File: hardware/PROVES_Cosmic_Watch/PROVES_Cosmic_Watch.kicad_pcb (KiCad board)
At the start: 4 copper layers, 88 x 95 mm, 43 parts, among them J1 USB_B_Micro, J2 DF11, J3 Conn_Coaxial, U2 LT3461, U3 LT1807, U4 MICROFC-60035-SMT-TR

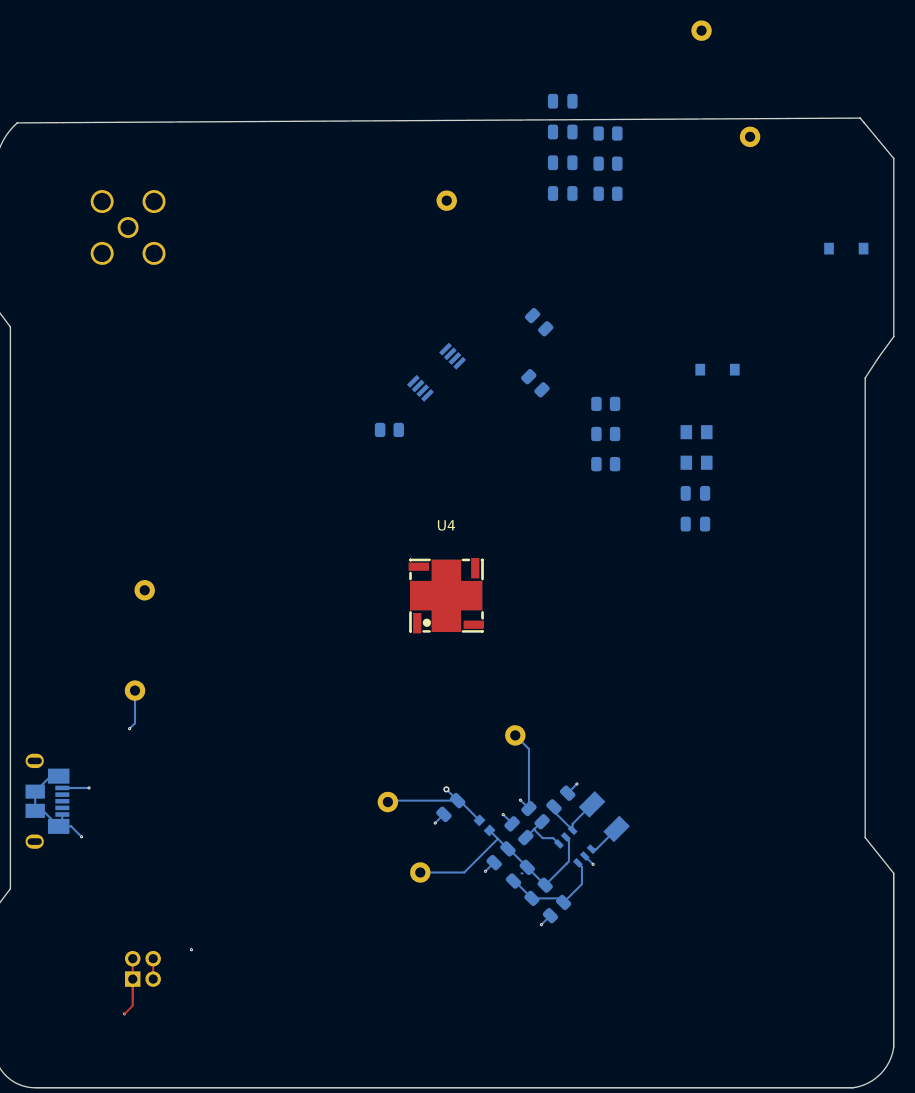
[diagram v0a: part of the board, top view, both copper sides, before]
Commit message: Finished Layout
Gotta redo it with Phyllis's new recommendations
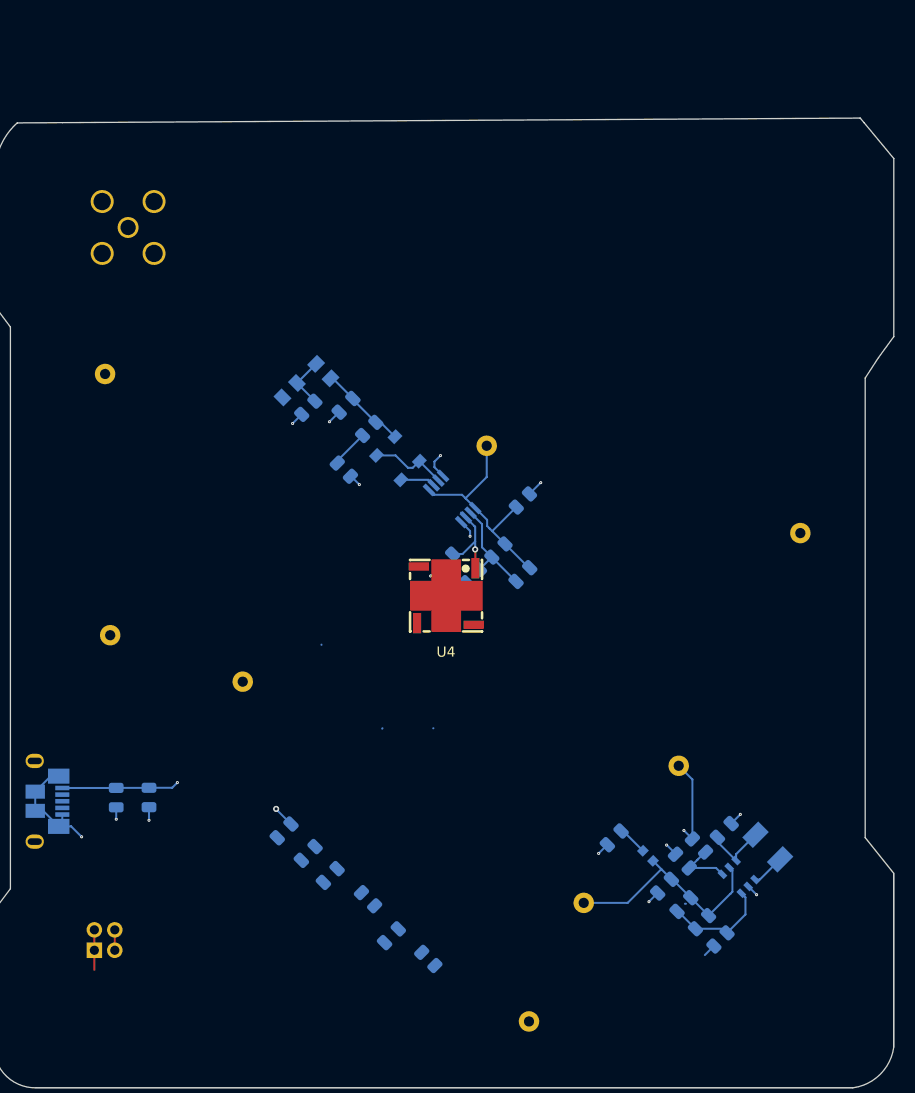
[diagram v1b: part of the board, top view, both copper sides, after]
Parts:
- added C14: 10uF, Capacitor_SMD:C_0805_2012Metric, B.Cu at (112.0, 113.0)
- added C15: 0.1uF, Capacitor_SMD:C_0805_2012Metric, B.Cu at (115.2, 113.0)
- C9: value .47uF -> 0.47uF
- L2: value BLM18 -> BLM18BD252SN1D
- TP2: value Post Processed Signal -> Post Processed Signal Test Point
- TP3: value GND Test Point -> GND
- TP7: value Bias V+ -> V+ Bias
- TP8: value V Out -> V+ Out
- U2: value LT3461 -> LT3461ES6-TRPBF
- moved TP3 79.4 mm to (111.4, 97.1)
- moved R12 77.0 mm to (142.5, 128.8), turned to -45 degrees
- moved C13 76.5 mm to (128.4, 116.3), turned to -135 degrees
- moved R13 75.8 mm to (136.6, 123.0), turned to -45 degrees
- moved C12 74.9 mm to (130.8, 118.5), turned to -135 degrees
- moved C10 74.6 mm to (138.9, 126.5), turned to -135 degrees
- moved C11 73.4 mm to (132.9, 120.6), turned to -135 degrees
- moved TP4 64.4 mm to (178.9, 87.1)
- moved D2 47.3 mm to (140.4, 78.9), turned to -45 degrees
- moved TP1 45.8 mm to (148.2, 78.5)
- moved R14 44.7 mm to (144.3, 89.8), turned to -135 degrees
- moved R6 40.0 mm to (128.9, 73.1), turned to -135 degrees
- moved C3 37.6 mm to (132.2, 71.2), turned to 135 degrees
- moved TP2 37.5 mm to (110.9, 71.5)
- moved C2 35.3 mm to (134.5, 74.6), turned to 45 degrees
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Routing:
- net Net-(U3B-+): track 0.00 -> 23.1 mm
- net Net-(U3A--): track 0.00 -> 10.7 mm
- net SiPM Signal: track 0.00 -> 8.75 mm, vias 0 -> 1
- net Net-(D2-K): track 0.00 -> 8.52 mm
- net GND: track 26.7 -> 35.2 mm, vias 8 -> 15
- net V_Bias: track 11.4 -> 2.94 mm, vias 1 -> 0
- net Net-(D1-K): track 0.00 -> 7.65 mm
- net +5V: track 28.0 -> 35.5 mm, vias 4 -> 3
- net Net-(D1-A): track 0.00 -> 7.16 mm
- net Net-(C3-Pad2): track 0.00 -> 5.16 mm
- net Net-(U4-CATHODE): track 0.00 -> 2.14 mm, vias 0 -> 1
- added copper zone on In1.Cu, net +5V
- added copper zone on In2.Cu, net GND

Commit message: Layout Updates
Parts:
- added C4: 10uF, Capacitor_SMD:C_0805_2012Metric_Pad1.18x1.45mm_HandSolder, F.Cu at (135.7, 81.2)
- added TP5: Bias Voltage, TestPoint:TestPoint_Keystone_5000-5004_Miniature, F.Cu at (96.1, 106.0)
- TP3: value GND -> GND Test Point
- TP6: value 5V -> 5V Test Point
- TP7: value V+ Bias -> FB Test Point
- TP8: value V+ Out -> Output Voltage Test Point
- TP9: value SHDN -> SHDN Test Point
- moved J1 66.4 mm to (171.5, 108.1), turned to 180 degrees
- moved J2 60.2 mm to (171.0, 128.4), turned to 0 degrees
- moved C14 53.7 mm to (165.5, 108.0), turned to 90 degrees
- moved C15 47.0 mm to (162.0, 108.1), turned to 90 degrees
- moved TP6 34.0 mm to (95.6, 119.8)
- moved TP7 30.2 mm to (122.2, 136.6)
- moved TP9 28.0 mm to (161.4, 137.3), turned to 0 degrees
- moved TP8 24.2 mm to (137.3, 136.1)
- moved TP1 23.7 mm to (131.8, 61.4)
- moved TP3 22.4 mm to (95.7, 113.2)
- moved L1 17.4 mm to (158.4, 118.8)
- moved L2 17.4 mm to (146.7, 119.7)
- moved C16 17.4 mm to (150.0, 120.2)
- moved C5 17.4 mm to (154.1, 117.2)
- moved C6 17.4 mm to (150.2, 124.5)
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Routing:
- net +5V: track 35.5 -> 10.2 mm, vias 3 -> 1
- net Post Processed Signal: track 0.00 -> 25.2 mm
- net GND: track 35.2 -> 17.1 mm, vias 15 -> 10
- net V_Out: track 22.5 -> 13.5 mm
- net Net-(U4-CATHODE): track 2.14 -> 10.6 mm
- net Net-(U3B-+): track 23.1 -> 17.1 mm
- net Net-(C10-Pad1): track 0.00 -> 4.44 mm
- net V_Bias: track 2.94 -> 5.72 mm
- net Net-(U3A--): track 10.7 -> 13.4 mm
- net SiPM Signal: track 8.75 -> 11.0 mm
- added copper zone on B.Cu, net +5V
- added copper zone on In1.Cu, net GND
- removed copper zone on In1.Cu, net +5V
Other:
- board size 88 x 95 mm -> 88 x 94.5 mm

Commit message: Layout Updates
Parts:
- moved C4 156.0 mm to (1.91, 1.00), turned to 0 degrees
- moved TP1 7.00 mm to (138.8, 61.3)
- moved TP5 2.75 mm to (95.7, 103.3)
- moved C14 0.42 mm to (165.5, 108.5)
- moved C15 0.42 mm to (162.0, 108.5)
- moved TP8 0.14 mm to (137.3, 136.3)
- moved TP4 0.07 mm to (168.6, 94.4)
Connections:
- TP9 pad 1: +5V -> Net-(U2-*SHDN)
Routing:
- net GND: track 17.1 -> 31.6 mm, vias 10 -> 17
- net +5V: track 10.2 -> 18.3 mm, vias 1 -> 0
- net SiPM Signal: track 11.0 -> 10.4 mm

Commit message: Layout Updates
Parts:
- removed TP9: SHDN Test Point, TestPoint:TestPoint_Keystone_5000-5004_Miniature
- added C7: 0.1uF, Capacitor_SMD:C_0805_2012Metric, B.Cu at (132.9, 79.9)
- C4: footprint Capacitor_SMD:C_0805_2012Metric_Pad1.18x1.45mm_HandSolder -> Capacitor_SMD:C_0805_2012Metric; moved to B.Cu
- TP2: value Post Processed Signal Test Point -> PPS
- TP3: value GND Test Point -> GND
- TP5: value Bias Voltage -> V+ Bias
- TP7: value FB Test Point -> Post FB
- TP8: value Output Voltage Test Point -> V+ Out
- moved C4 150.8 mm to (131.3, 78.5), turned to -135 degrees
- moved TP4 71.8 mm to (96.8, 94.2)
- moved TP3 29.4 mm to (101.7, 142.0)
- moved TP2 18.0 mm to (96.5, 87.3)
- moved TP6 16.7 mm to (101.7, 135.4)
- moved TP1 3.69 mm to (136.0, 63.8)
- moved R14 2.09 mm to (132.5, 91.5), turned to 135 degrees
- moved TP5 1.64 mm to (96.9, 104.4)
- moved TP7 1.23 mm to (123.2, 135.9)
- moved TP8 0.60 mm to (136.8, 135.9)
- moved D1 0.33 mm to (127.8, 84.1), turned to 135 degrees
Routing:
- net SiPM Signal: track 10.4 -> 50.6 mm
- net Net-(U4-CATHODE): track 10.6 -> 44.8 mm
- net V_Bias: track 5.72 -> 33.6 mm
- net Post Processed Signal: track 25.2 -> 49.9 mm
- net Net-(U3B-+): track 17.1 -> 41.7 mm
- net V_Out: track 13.5 -> 32.1 mm
- net GND: track 31.6 -> 48.7 mm, vias 17 -> 18
- net Net-(D1-A): track 7.16 -> 16.4 mm
- net +5V: track 18.3 -> 24.7 mm
- net Net-(D1-K): track 7.65 -> 4.92 mm

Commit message: Layout Updates
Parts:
- added H1: MountingHole, MountingHole:MountingHole_2.7mm_M2.5, F.Cu at (105.0, 71.0)
- added H2: MountingHole, MountingHole:MountingHole_2.7mm_M2.5, F.Cu at (161.2, 71.1)
- added H3: MountingHole, MountingHole:MountingHole_2.7mm_M2.5, F.Cu at (105.0, 127.1)
- added H4: MountingHole, MountingHole:MountingHole_2.7mm_M2.5, F.Cu at (161.0, 127.1)
- TP1, TP2, TP3, TP7, TP8: moved to F.Cu
- TP4: value SiPM Signal -> SiPM; moved to F.Cu
- TP6: value 5V Test Point -> 5V; moved to F.Cu
- moved TP6 80.9 mm to (170.1, 92.1)
- moved TP2 42.1 mm to (128.2, 59.6), turned to 180 degrees
- moved J3 17.5 mm to (116.9, 59.5), turned to 0 degrees
- moved TP3 7.29 mm to (106.2, 136.3)
- moved R6 5.25 mm to (117.7, 71.6), turned to 135 degrees
- moved R7 2.52 mm to (118.0, 76.7)
- moved J1 0.07 mm to (171.5, 108.2)
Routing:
- net Post Processed Signal: track 49.9 -> 27.2 mm
- net GND: track 48.7 -> 43.7 mm
- net +5V: track 24.7 -> 20.0 mm
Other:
- outline, holes or cut-outs redrawn
- board text added: "5V"

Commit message: silkscreens and layout updates
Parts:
- added G***: LOGO, LOGO, F.Cu at (161.6, 59.5)
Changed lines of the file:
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@@
 		)
+	)
+	(footprint "LOGO"
+		(layer "F.Cu")
+		(at 161.63 59.47)
+		(property "Reference" "G***"
+			(at 11.8 1.87 0)
+			(layer "F.SilkS")
+			(hide yes)
+			(effects
+				(font
+					(size 1.5 1.5)
+					(thickness 0.3)
+				)
+			)
+		)
+		(property "Value" "LOGO"
+			(at 0.75 0 0)
+			(layer "F.SilkS")
+			(hide yes)
+			(effects
+				(font
+					(size 1.5 1.5)
+					(thickness 0.3)
+				)
+			)
+		)
+		(property "Datasheet" ""
+			(at 0 0 0)
+			(layer "F.Fab")
+			(hide yes)
+			(effects
+				(font
+					(size 1.27 1.27)
+					(thickness 0.15)
+				)
+			)
+		)
+		(property "Description" ""
+			(at 0 0 0)
+			(layer "F.Fab")
+			(hide yes)
+			(effects
+				(font
+					(size 1.27 1.27)
+					(thickness 0.15)
+				)
+			)
+		)
+		(attr board_only exclude_from_pos_files exclude_from_bom)
+		(fp_poly
+			(pts
+				(xy -0.450888 1.277514) (xy -0.475938 1.302564) (xy -0.500987 1.277514) (xy -0.475938 1.252465)
+			)
+			(stroke
+				(width 0)
+				(type solid)
+			)
+			(fill yes)
+			(layer "F.SilkS")
+		)
+		(fp_poly
+			(pts
+				(xy 1.703352 2.429782) (xy 1.678303 2.454832) (xy 1.653254 2.429782) (xy 1.678303 2.404733)
+			)
+			(stroke
+				(width 0)
+				(type solid)
+			)
+			(fill yes)
+			(layer "F.SilkS")
+		)
+		(fp_poly
+			(pts
+				(xy 3.279211 0.0395) (xy 3.300407 0.113033) (xy 3.307967 0.258841) (xy 3.303235 0.450131) (xy 3.287558 0.660107)
+				(xy 3.26228 0.861974) (xy 3.229712 1.02527) (xy 3.13549 1.308957) (xy 3.009734 1.57839) (xy 2.868867 1.801694)
+				(xy 2.773906 1.909916) (xy 2.655226 2.02141) (xy 2.655226 1.856247) (xy 2.646449 1.748991) (xy 2.615246 1.7274)
+				(xy 2.592603 1.741532) (xy 2.501541 1.786993) (xy 2.369207 1.826355) (xy 2.366768 1.82688) (xy 2.217808 1.89568)
+				(xy 2.078411 2.044493) (xy 2.05788 2.073515) (xy 1.95687 2.210647) (xy 1.865029 2.319544) (xy 1.83115 2.352517)
+				(xy 1.81432 2.350836) (xy 1.847798 2.282) (xy 1.924336 2.16087) (xy 1.925484 2.159163) (xy 2.105508 1.83183)
+				(xy 2.193322 1.517767) (xy 2.204059 1.3639) (xy 2.199553 1.254119) (xy 2.167473 1.226673) (xy 2.080783 1.2637)
+				(xy 2.064836 1.271933) (xy 1.917773 1.330869) (xy 1.747349 1.377344) (xy 1.733154 1.380125) (xy 1.540975 1.416178)
+				(xy 1.77642 1.127115) (xy 1.912331 0.947679) (xy 2.03682 0.761983) (xy 2.118085 0.61942) (xy 2.190952 0.485907)
+				(xy 2.259533 0.421419) (xy 2.35558 0.401487) (xy 2.402191 0.400509) (xy 2.690185 0.366549) (xy 2.944025 0.272846)
+				(xy 3.112442 0.151674) (xy 3.20652 0.069893) (xy 3.270181 0.036892)
+			)
+			(stroke
+				(width 0)
+				(type solid)
+			)
+			(fill yes)
+			(layer "F.SilkS")
+		)
+		(fp_poly
+			(pts
+				(xy -1.534541 -2.910684) (xy -1.264983 -2.786697) (xy -1.034242 -2.599458) (xy -0.865006 -2.365667)
+				(xy -0.800828 -2.20434) (xy -0.754476 -1.853307) (xy -0.79986 -1.466782) (xy -0.936385 -1.048185)
+				(xy -1.042062 -0.821198) (xy -1.116458 -0.693239) (xy -1.234357 -0.517662) (xy -1.400641 -0.287776)
+				(xy -1.620189 0.003108) (xy -1.897883 0.361679) (xy -2.00235 0.495029) (xy -2.244475 0.839501) (xy -2.413872 1.160571)
+				(xy -2.507233 1.449481) (xy -2.521253 1.697476) (xy -2.496962 1.804878) (xy -2.456872 1.896874)
+				(xy -2.418436 1.916775) (xy -2.37297 1.857476) (xy -2.31179 1.711868) (xy -2.281095 1.628205) (xy -2.068904 1.181266)
+				(xy -1.768702 0.762572) (xy -1.390873 0.381445) (xy -0.945802 0.047205) (xy -0.443871 -0.230826)
+				(xy -0.018235 -0.403134) (xy 0.265499 -0.485785) (xy 0.618151 -0.56557) (xy 1.008479 -0.636785)
+				(xy 1.405243 -0.693724) (xy 1.773866 -0.730441) (xy 2.270218 -0.766366) (xy 2.241148 -0.420757)
+				(xy 2.148822 0.092771) (xy 1.962484 0.592882) (xy 1.729892 1.001972) (xy 1.599268 1.189432) (xy 1.49076 1.317339)
+				(xy 1.374749 1.411945) (xy 1.221613 1.499503) (xy 1.102169 1.558337) (xy 0.775341 1.74731) (xy 0.522625 1.960756)
+				(xy 0.512478 1.97165) (xy 0.399118 2.092168) (xy 0.315158 2.176256) (xy 0.281028 2.204339) (xy 0.263184 2.159435)
+				(xy 0.233799 2.042186) (xy 0.202053 1.891862) (xy 0.138058 1.626128) (xy 0.058877 1.431845) (xy -0.049866 1.280269)
+				(xy -0.152341 1.183284) (xy -0.293267 1.093572) (xy -0.427875 1.054771) (xy -0.529182 1.07137) (xy -0.56464 1.114694)
+				(xy -0.603925 1.141457) (xy -0.685398 1.089469) (xy -0.694062 1.08188) (xy -0.766311 1.020566) (xy -0.793691 1.015796)
+				(xy -0.780261 1.08059) (xy -0.735109 1.213527) (xy -0.6331 1.390242) (xy -0.501757 1.514119) (xy -0.418268 1.576048)
+				(xy -0.3585 1.642783) (xy -0.311539 1.736943) (xy -0.266472 1.881145) (xy -0.212385 2.098008) (xy -0.204959 2.129191)
+				(xy -0.117754 2.415395) (xy -0.007748 2.651733) (xy 0.114891 2.819023) (xy 0.192819 2.879658) (xy 0.235547 2.907212)
+				(xy 0.237707 2.926475) (xy 0.187611 2.938685) (xy 0.073568 2.945077) (xy -0.116111 2.946886) (xy -0.393117 2.945348)
+				(xy -0.425839 2.94506) (xy -0.711065 2.941361) (xy -0.979673 2.935824) (xy -1.206695 2.929107) (xy -1.367162 2.921866)
+				(xy -1.402762 2.919348) (xy -1.766622 2.880765) (xy -2.101764 2.830091) (xy -2.389668 2.771042)
+				(xy -2.611816 2.707336) (xy -2.735982 2.651761) (xy -2.978224 2.445588) (xy -3.154224 2.176498)
+				(xy -3.256724 1.862572) (xy -3.278461 1.521891) (xy -3.257741 1.352343) (xy -3.173447 1.059026)
+				(xy -3.027009 0.724671) (xy -2.83164 0.374281) (xy -2.600551 0.032856) (xy -2.476921 -0.125247)
+				(xy -2.318623 -0.31934) (xy -2.16673 -0.508596) (xy -2.043988 -0.66455) (xy -1.998115 -0.724522)
+				(xy -1.911672 -0.84396) (xy -1.880779 -0.912537) (xy -1.900283 -0.959109) (xy -1.948905 -1.000064)
+				(xy -2.01641 -1.066933) (xy -2.00508 -1.132035) (xy -1.973694 -1.177318) (xy -1.918393 -1.241675)
+				(xy -1.873827 -1.23785) (xy -1.804817 -1.160831) (xy -1.79792 -1.152269) (xy -1.69636 -1.017017)
+				(xy -1.600218 -0.876726) (xy -1.534475 -0.790444) (xy -1.506806 -0.786818) (xy -1.518077 -0.855473)
+				(xy -1.569156 -0.986032) (xy -1.587738 -1.026061) (xy -1.635884 -1.140364) (xy -1.646588 -1.232632)
+				(xy -1.619824 -1.347514) (xy -1.58749 -1.441075) (xy -1.520543 -1.704146) (xy -1.519538 -1.922416)
+				(xy -1.581111 -2.085188) (xy -1.701897 -2.18177) (xy -1.827646 -2.20434) (xy -1.943706 -2.170103)
+				(xy -1.99127 -2.079068) (xy -1.969052 -1.948749) (xy -1.875767 -1.796662) (xy -1.859027 -1.776972)
+				(xy -1.739947 -1.614268) (xy -1.703591 -1.494676) (xy -1.750006 -1.42283) (xy -1.855222 -1.402762)
+				(xy -1.978091 -1.426265) (xy -2.035927 -1.47791) (xy -2.103346 -1.544562) (xy -2.142317 -1.553058)
+				(xy -2.188928 -1.542276) (xy -2.166066 -1.495274) (xy -2.131019 -1.454879) (xy -2.077956 -1.349104)
+				(xy -2.073019 -1.230515) (xy -2.111229 -1.136045) (xy -2.178575 -1.10217) (xy -2.265902 -1.140229)
+				(xy -2.384111 -1.238104) (xy -2.509873 -1.371346) (xy -2.619862 -1.515507) (xy -2.685866 -1.633856)
+				(xy -2.756866 -1.920312) (xy -2.739293 -2.200462) (xy -2.64363 -2.458313) (xy -2.480358 -2.677869)
+				(xy -2.259959 -2.843139) (xy -1.992915 -2.938127) (xy -1.820229 -2.954719)
+			)
+			(stroke
+				(width 0)
+				(type solid)
+			)
+			(fill yes)
+			(layer "F.SilkS")
+		)
+		(embedded_fonts no)
 	)
 	(footprint "Capacitor_SMD:C_0805_2012Metric"

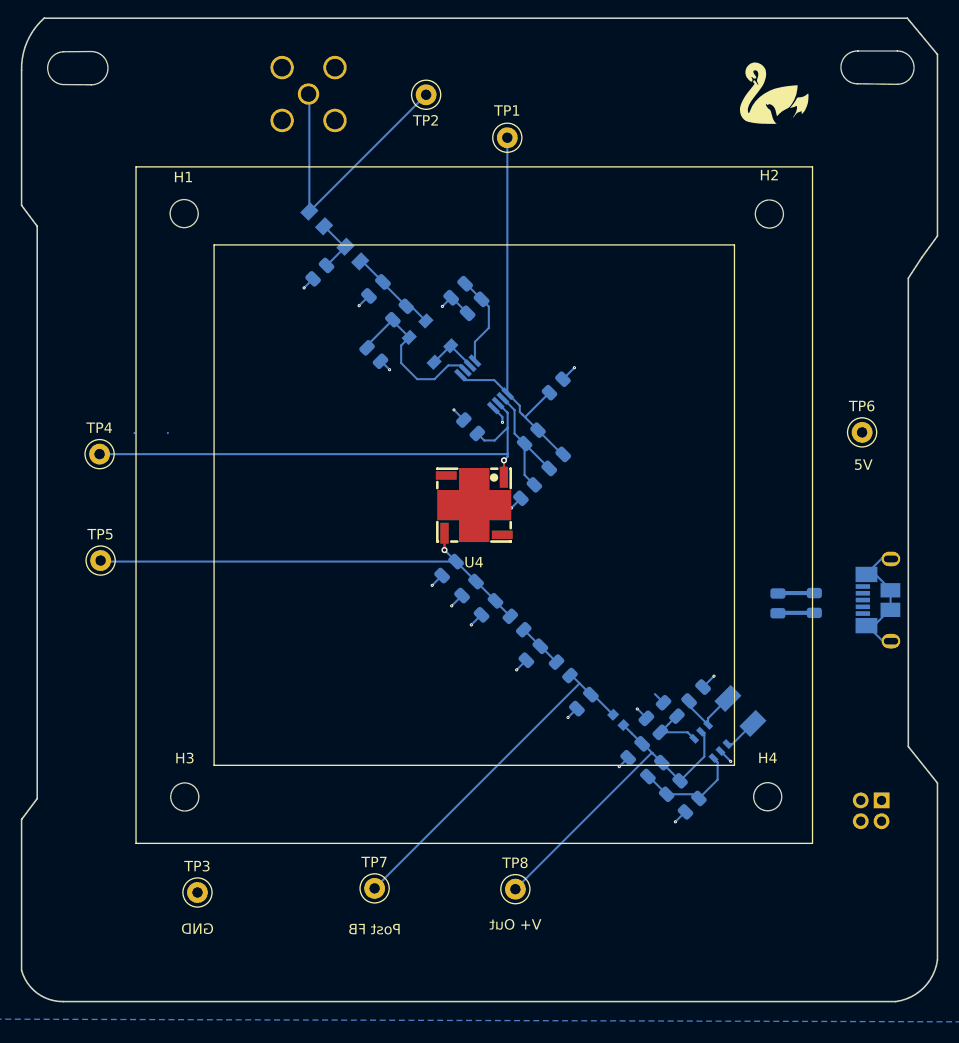
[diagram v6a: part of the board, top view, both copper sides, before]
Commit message: silkscreen, mounting holes and logo
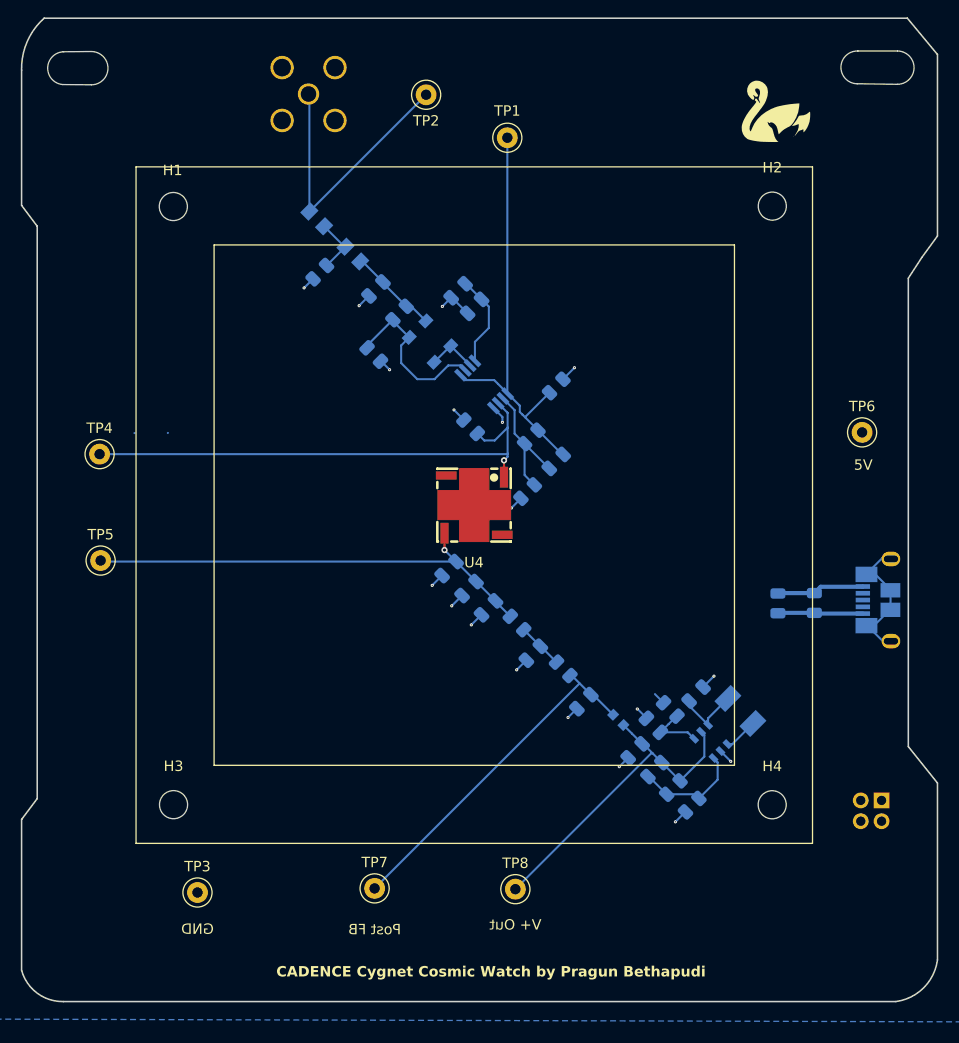
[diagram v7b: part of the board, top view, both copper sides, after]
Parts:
- added G***: LOGO, LOGO, F.Cu at (146.8, 57.8)
- moved G*** 1.75 mm to (161.8, 61.2)
- moved H3 1.31 mm to (103.9, 127.8)
- moved H1 1.24 mm to (103.9, 70.4)
- moved H4 0.88 mm to (161.4, 127.8)
- moved H2 0.81 mm to (161.5, 70.3)
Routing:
- net GND: track 43.7 -> 48.7 mm
- net +5V: track 20.0 -> 24.7 mm
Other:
- board text added: "CADENCE Cygnet Cosmic Watch by Pragun Bethapudi"
